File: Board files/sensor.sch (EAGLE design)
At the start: 33 parts, among them Q1 BCM847DS, U1 TL974, U2 TL974

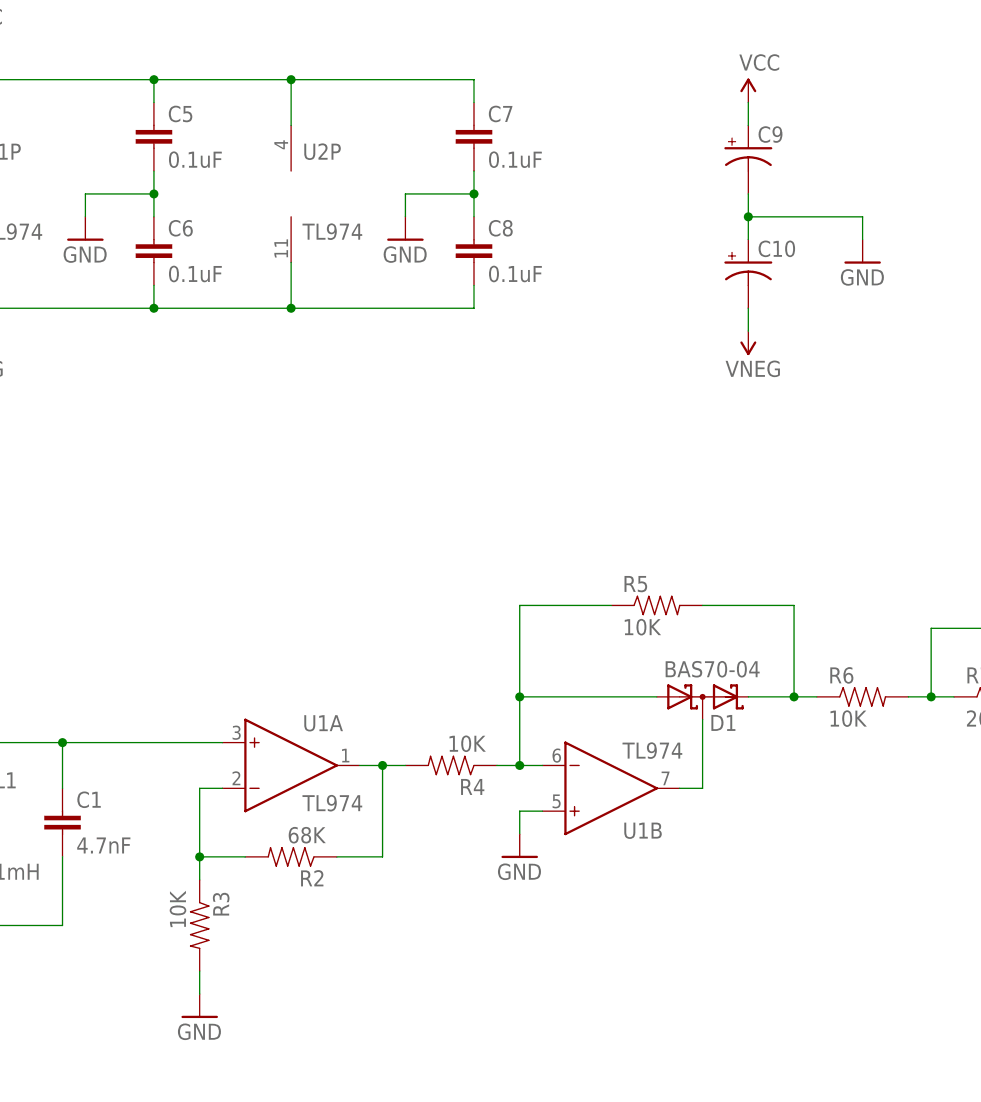
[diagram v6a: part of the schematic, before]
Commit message: Increased initial sensor gain from 8 to 256
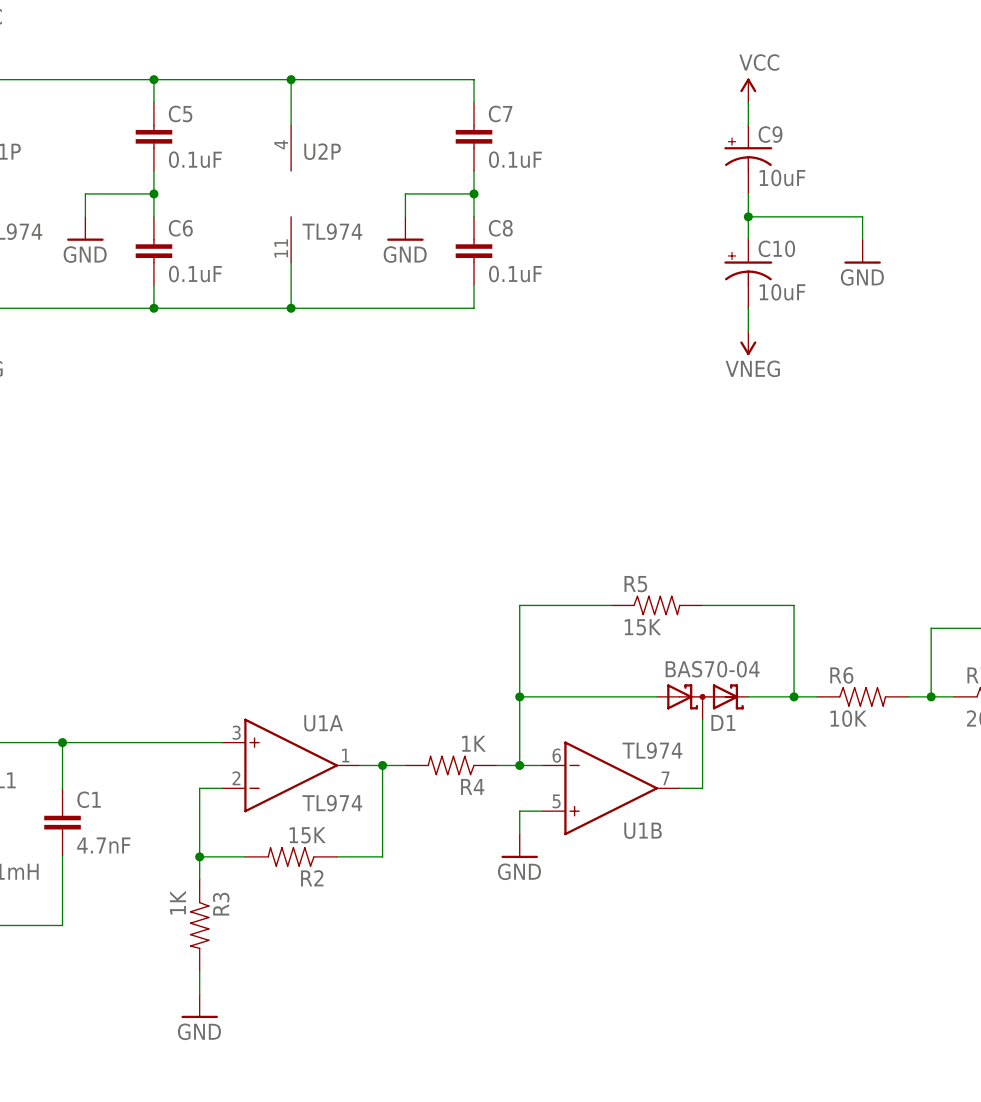
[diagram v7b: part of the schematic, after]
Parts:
- C10, C9: value (none) -> 10uF
- R2: value 68K -> 15K
- R3, R4: value 10K -> 1K
- R5: value 10K -> 15K
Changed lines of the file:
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@@
 <part name="R1" library="SparkFun-Resistors" deviceset="RESISTOR" device="0805-RES" value="1K"/>
 <part name="C1" library="SparkFun-Capacitors" deviceset="CAP" device="0805" value="4.7nF"/>
-<part name="R2" library="SparkFun-Resistors" deviceset="RESISTOR" device="0805-RES" value="68K"/>
-<part name="R3" library="SparkFun-Resistors" deviceset="RESISTOR" device="0805-RES" value="10K"/>
+<part name="R2" library="SparkFun-Resistors" deviceset="RESISTOR" device="0805-RES" value="15K"/>
+<part name="R3" library="SparkFun-Resistors" deviceset="RESISTOR" device="0805-RES" value="1K"/>
 <part name="GND4" library="SparkFun-Aesthetics" deviceset="GND" device=""/>
 <part name="GND5" library="SparkFun-Aesthetics" deviceset="GND" device=""/>
 <part name="GND7" library="SparkFun-Aesthetics" deviceset="GND" device=""/>
-<part name="R4" library="SparkFun-Resistors" deviceset="RESISTOR" device="0805-RES" value="10K"/>
-<part name="R5" library="SparkFun-Resistors" deviceset="RESISTOR" device="0805-RES" value="10K"/>
+<part name="R4" library="SparkFun-Resistors" deviceset="RESISTOR" device="0805-RES" value="1K"/>
+<part name="R5" library="SparkFun-Resistors" deviceset="RESISTOR" device="0805-RES" value="15K"/>
 <part name="R6" library="SparkFun-Resistors" deviceset="RESISTOR" device="0805-RES" value="10K"/>
 <part name="C2" library="SparkFun-Capacitors" deviceset="CAP" device="0805" value="0.1uF"/>
@@
 <part name="GND14" library="SparkFun-Aesthetics" deviceset="GND" device=""/>
 <part name="GND15" library="SparkFun-Aesthetics" deviceset="GND" device=""/>
-<part name="C9" library="resistor" deviceset="CPOL-US" device="E2-4"/>
-<part name="C10" library="resistor" deviceset="CPOL-US" device="E2-4"/>
+<part name="C9" library="resistor" deviceset="CPOL-US" device="E2-4" value="10uF"/>
+<part name="C10" library="resistor" deviceset="CPOL-US" device="E2-4" value="10uF"/>
 <part name="SUPPLY7" library="SparkFun-Aesthetics" deviceset="VCC" device=""/>
 <part name="SUPPLY8" library="SparkFun-Aesthetics" deviceset="VNEG" device=""/>

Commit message: Switched to polarized connectors
Also added 3.3v out pins on logic board, various other changes
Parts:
- JP1: device SparkFun-Connectors:M04LOCK_LONGPADS -> SparkFun-Connectors:M04POLAR_LOCK
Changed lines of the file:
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@@
 </classes>
 <parts>
-<part name="JP1" library="SparkFun-Connectors" deviceset="M04" device="LOCK_LONGPADS"/>
+<part name="JP1" library="SparkFun-Connectors" deviceset="M04" device="POLAR_LOCK"/>
 <part name="SUPPLY1" library="SparkFun-Aesthetics" deviceset="VCC" device=""/>
 <part name="SUPPLY2" library="SparkFun-Aesthetics" deviceset="VCC" device=""/>
